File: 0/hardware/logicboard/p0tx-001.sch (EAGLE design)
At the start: 33 parts, among them IC1 LTC485N, IC2 LTC485N, IC3 LTC485N, J0 DC5V, J7 DIN5, J8 DIN5, J9 DIN5, X9 NELTRON-7810-XPXC

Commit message: Redesign.
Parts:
- removed LED2: YELLOW, led:LED3MM
- added C7: 10n, rcl:C-EU025-024X044
- added IC4: LTC485N, linear-technology:LTC485N
- added J10: DIN5, SparkFun-Connectors:DIN5
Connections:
- removed net MNTRRTN: D4.A, OK2B.C2, X9.8
- removed net MNTRSND: R4.1, X9.7
- removed net N$11: LED2.C, OK2B.VO2
- removed net N$12: LED2.A, R6L2.1
- new net MI4RTN: D4.A, J10.5, OK2B.C2
- new net MI4SND: J10.4, R4.1
- new net N$6: IC4.DI, OK2B.VO2, RN2.5
- new net TX4+: IC4.A, X9.7
- new net TX4-: IC4.B, X9.8
- net GND: now also C7.2, IC4.GND
- net VCC: now also C7.1, IC4.!RE, IC4.DE, IC4.VCC; no longer R6L2.2
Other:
- moved on the sheet: C1, C2, C3, C4, C5, C6, D4, LED1, OK2B, R4, R5L1, R6L2

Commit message: Layout.
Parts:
- removed R2, R3, R4: 220, rcl:R-EU_0204/5
- removed R5L1, R6L2, R7X, R8X: 1k, rcl:R-EU_0204/5
- added RN1: 221, resistor-dil:8R-N
- R1: value 220 -> 1k
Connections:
- net MI1SND: now also RN1A.1; no longer R1.1
- net MI2SND: now also RN1B.1; no longer R2.1
- net MI3SND: now also RN1C.1; no longer R3.1
- net MI4SND: now also RN1D.1; no longer R4.1
- net MIDIIN: now also RN1A.2; no longer R1.2
- net N$1: now also RN1D.2; no longer R4.2
- net N$4: now also R1.1; no longer R5L1.1
- net N$7: now also RN1B.2; no longer R2.2
- net N$8: now also RN1C.2; no longer R3.2
- net VCC: now also R1.2; no longer R5L1.2
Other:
- moved on the sheet: R1
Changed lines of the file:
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@@
 <part name="SUPPLY29" library="supply2" library_urn="urn:adsk.eagle:library:372" deviceset="GND" device=""/>
 <part name="X9" library="con-rj45" deviceset="NELTRON-7810-XPXC" device=""/>
-<part name="R6L2" library="rcl" library_urn="urn:adsk.eagle:library:334" deviceset="R-EU_" device="0204/5" package3d_urn="urn:adsk.eagle:package:23488/1" value="1k"/>
-<part name="R1" library="rcl" library_urn="urn:adsk.eagle:library:334" deviceset="R-EU_" device="0204/5" package3d_urn="urn:adsk.eagle:package:23488/1" value="220"/>
-<part name="R4" library="rcl" library_urn="urn:adsk.eagle:library:334" deviceset="R-EU_" device="0204/5" package3d_urn="urn:adsk.eagle:package:23488/1" value="220"/>
-<part name="R5L1" library="rcl" library_urn="urn:adsk.eagle:library:334" deviceset="R-EU_" device="0204/5" package3d_urn="urn:adsk.eagle:package:23488/1" value="1k"/>
-<part name="R2" library="rcl" library_urn="urn:adsk.eagle:library:334" deviceset="R-EU_" device="0204/5" package3d_urn="urn:adsk.eagle:package:23488/1" value="220"/>
-<part name="R3" library="rcl" library_urn="urn:adsk.eagle:library:334" deviceset="R-EU_" device="0204/5" package3d_urn="urn:adsk.eagle:package:23488/1" value="220"/>
-<part name="R7X" library="rcl" library_urn="urn:adsk.eagle:library:334" deviceset="R-EU_" device="0204/5" package3d_urn="urn:adsk.eagle:package:23488/1" value="1k"/>
-<part name="R8X" library="rcl" library_urn="urn:adsk.eagle:library:334" deviceset="R-EU_" device="0204/5" package3d_urn="urn:adsk.eagle:package:23488/1" value="1k"/>
+<part name="R1" library="rcl" library_urn="urn:adsk.eagle:library:334" deviceset="R-EU_" device="0204/5" package3d_urn="urn:adsk.eagle:package:23488/1" value="1k"/>
 <part name="OK2" library="optocoupler" library_urn="urn:adsk.eagle:library:320" deviceset="HCPL2630" device="" package3d_urn="urn:adsk.eagle:package:21941/1"/>
 <part name="D2" library="SparkFun-DiscreteSemi" library_urn="urn:adsk.eagle:library:514" deviceset="DIODE" device="-1N4148" package3d_urn="urn:adsk.eagle:package:38452/1" value=""/>
@@
 <part name="SUPPLY30" library="supply2" library_urn="urn:adsk.eagle:library:372" deviceset="VCC" device=""/>
 <part name="SUPPLY31" library="supply2" library_urn="urn:adsk.eagle:library:372" deviceset="GND" device=""/>
+<part name="RN1" library="resistor-dil" library_urn="urn:adsk.eagle:library:342" deviceset="8R-N" device="" package3d_urn="urn:adsk.eagle:package:922/2" value="221"/>
 </parts>
 <sheets>
@@
 <attribute name="VALUE" x="201.93" y="108.458" size="1.778" layer="96"/>
 </instance>
-<instance part="R6L2" gate="G$1" x="134.62" y="20.32" smashed="yes">
-<attribute name="NAME" x="130.81" y="21.8186" size="1.778" layer="95"/>
-<attribute name="VALUE" x="130.81" y="17.018" size="1.778" layer="96"/>
-</instance>
-<instance part="R1" gate="G$1" x="76.2" y="127" smashed="yes">
-<attribute name="NAME" x="72.39" y="128.4986" size="1.778" layer="95"/>
-<attribute name="VALUE" x="72.39" y="123.698" size="1.778" layer="96"/>
-</instance>
-<instance part="R4" gate="G$1" x="76.2" y="38.1" smashed="yes">
-<attribute name="NAME" x="72.39" y="39.5986" size="1.778" layer="95"/>
-<attribute name="VALUE" x="72.39" y="34.798" size="1.778" layer="96"/>
-</instance>
-<instance part="R5L1" gate="G$1" x="60.96" y="157.48" smashed="yes" rot="R90">
+<instance part="R1" gate="G$1" x="60.96" y="157.48" smashed="yes" rot="R90">
 <attribute name="NAME" x="59.4614" y="153.67" size="1.778" layer="95" rot="R90"/>
 <attribute name="VALUE" x="64.262" y="153.67" size="1.778" layer="96" rot="R90"/>
-</instance>
-<instance part="R2" gate="G$1" x="76.2" y="99.06" smashed="yes">
-<attribute name="NAME" x="72.39" y="100.5586" size="1.778" layer="95"/>
-<attribute name="VALUE" x="72.39" y="95.758" size="1.778" layer="96"/>
-</instance>
-<instance part="R3" gate="G$1" x="76.2" y="68.58" smashed="yes">
-<attribute name="NAME" x="72.39" y="70.0786" size="1.778" layer="95"/>
-<attribute name="VALUE" x="72.39" y="65.278" size="1.778" layer="96"/>
-</instance>
-<instance part="R7X" gate="G$1" x="114.3" y="22.86" smashed="yes">
-<attribute name="NAME" x="110.49" y="24.3586" size="1.778" layer="95"/>
-<attribute name="VALUE" x="110.49" y="19.558" size="1.778" layer="96"/>
-</instance>
-<instance part="R8X" gate="G$1" x="114.3" y="12.7" smashed="yes">
-<attribute name="NAME" x="110.49" y="14.1986" size="1.778" layer="95"/>
-<attribute name="VALUE" x="110.49" y="9.398" size="1.778" layer="96"/>
 </instance>
 <instance part="OK2" gate="A" x="114.3" y="66.04" smashed="yes">
@@
 <instance part="SUPPLY31" gate="GND" x="243.84" y="63.5" smashed="yes">
 <attribute name="VALUE" x="241.935" y="60.325" size="1.778" layer="96"/>
+</instance>
+<instance part="RN1" gate="A" x="76.2" y="127" smashed="yes">
+<attribute name="VALUE" x="78.74" y="123.952" size="1.778" layer="96"/>
+<attribute name="NAME" x="71.12" y="123.952" size="1.778" layer="95"/>
+</instance>
+<instance part="RN1" gate="B" x="76.2" y="99.06" smashed="yes">
+<attribute name="VALUE" x="78.74" y="96.012" size="1.778" layer="96"/>
+<attribute name="NAME" x="71.12" y="96.012" size="1.778" layer="95"/>
+</instance>
+<instance part="RN1" gate="C" x="76.2" y="68.58" smashed="yes">
+<attribute name="VALUE" x="78.74" y="65.532" size="1.778" layer="96"/>
+<attribute name="NAME" x="71.12" y="65.532" size="1.778" layer="95"/>
+</instance>
+<instance part="RN1" gate="D" x="76.2" y="38.1" smashed="yes">
+<attribute name="VALUE" x="78.74" y="35.052" size="1.778" layer="96"/>
+<attribute name="NAME" x="71.12" y="35.052" size="1.778" layer="95"/>
+</instance>
+<instance part="RN1" gate="E" x="231.14" y="124.46" smashed="yes">
+<attribute name="VALUE" x="233.68" y="121.412" size="1.778" layer="96"/>
+<attribute name="NAME" x="226.06" y="121.412" size="1.778" layer="95"/>
+</instance>
+<instance part="RN1" gate="F" x="231.14" y="119.38" smashed="yes">
+<attribute name="VALUE" x="233.68" y="116.332" size="1.778" layer="96"/>
+<attribute name="NAME" x="226.06" y="116.332" size="1.778" layer="95"/>
+</instance>
+<instance part="RN1" gate="G" x="231.14" y="114.3" smashed="yes">
+<attribute name="VALUE" x="233.68" y="111.252" size="1.778" layer="96"/>
+<attribute name="NAME" x="226.06" y="111.252" size="1.778" layer="95"/>
+</instance>
+<instance part="RN1" gate="H" x="231.14" y="109.22" smashed="yes">
+<attribute name="VALUE" x="233.68" y="106.172" size="1.778" layer="96"/>
+<attribute name="NAME" x="226.06" y="106.172" size="1.778" layer="95"/>
 </instance>
 </instances>
@@
 <segment>
 <pinref part="SUPPLY28" gate="G$1" pin="VCC"/>
-<pinref part="R5L1" gate="G$1" pin="2"/>
+<pinref part="R1" gate="G$1" pin="2"/>
 <wire x1="60.96" y1="162.56" x2="60.96" y2="165.1" width="0.1524" layer="91"/>
 </segment>
@@
 <wire x1="81.28" y1="127" x2="96.52" y2="127" width="0.1524" layer="91"/>
 <junction x="96.52" y="127"/>
-<pinref part="R1" gate="G$1" pin="2"/>
+<pinref part="RN1" gate="A" pin="2"/>
 </segment>
 </net>
@@
 <segment>
 <pinref part="J7" gate="G$1" pin="4"/>
-<pinref part="R1" gate="G$1" pin="1"/>
 <wire x1="71.12" y1="127" x2="33.02" y2="127" width="0.1524" layer="91"/>
 <label x="50.8" y="127" size="1.778" layer="95"/>
+<pinref part="RN1" gate="A" pin="1"/>
 </segment>
 </net>
@@
 <segment>
 <pinref part="J8" gate="G$1" pin="4"/>
-<pinref part="R2" gate="G$1" pin="1"/>
 <wire x1="33.02" y1="99.06" x2="71.12" y2="99.06" width="0.1524" layer="91"/>
 <label x="50.8" y="99.06" size="1.778" layer="95"/>
+<pinref part="RN1" gate="B" pin="1"/>
 </segment>
 </net>
 <net name="N$7" class="0">
 <segment>
-<pinref part="R2" gate="G$1" pin="2"/>
 <pinref part="OK1" gate="B" pin="A2"/>
 <wire x1="81.28" y1="99.06" x2="96.52" y2="99.06" width="0.1524" layer="91"/>
@@
 <wire x1="96.52" y1="96.52" x2="96.52" y2="99.06" width="0.1524" layer="91"/>
 <junction x="96.52" y="99.06"/>
+<pinref part="RN1" gate="B" pin="2"/>
 </segment>
 </net>
@@
 <segment>
 <pinref part="OK2" gate="A" pin="A1"/>
-<pinref part="R3" gate="G$1" pin="2"/>
 <wire x1="101.6" y1="68.58" x2="96.52" y2="68.58" width="0.1524" layer="91"/>
 <pinref part="D3" gate="G$1" pin="C"/>
@@
 <wire x1="96.52" y1="66.04" x2="96.52" y2="68.58" width="0.1524" layer="91"/>
 <junction x="96.52" y="68.58"/>
+<pinref part="RN1" gate="C" pin="2"/>
 </segment>
 </net>
 <net name="MI3SND" class="0">
 <segment>
-<pinref part="R3" gate="G$1" pin="1"/>
 <pinref part="J9" gate="G$1" pin="4"/>
 <wire x1="71.12" y1="68.58" x2="33.02" y2="68.58" width="0.1524" layer="91"/>
 <label x="50.8" y="68.58" size="1.778" layer="95"/>
+<pinref part="RN1" gate="C" pin="1"/>
 </segment>
 </net>
 <net name="N$1" class="0">
 <segment>
-<pinref part="R4" gate="G$1" pin="2"/>
 <pinref part="OK2" gate="B" pin="A2"/>
 <wire x1="81.28" y1="38.1" x2="96.52" y2="38.1" width="0.1524" layer="91"/>
@@
 <pinref part="D4" gate="G$1" pin="C"/>
 <wire x1="96.52" y1="35.56" x2="93.98" y2="35.56" width="0.1524" layer="91"/>
+<pinref part="RN1" gate="D" pin="2"/>
 </segment>
 </net>
@@
 <net name="N$4" class="0">
 <segment>
-<pinref part="R5L1" gate="G$1" pin="1"/>
+<pinref part="R1" gate="G$1" pin="1"/>
 <pinref part="LED1" gate="G$1" pin="A"/>
 <wire x1="60.96" y1="152.4" x2="60.96" y2="149.86" width="0.1524" layer="91"/>
@@
 <net name="MI4SND" class="0">
 <segment>
-<pinref part="R4" gate="G$1" pin="1"/>
 <pinref part="J10" gate="G$1" pin="4"/>
 <wire x1="71.12" y1="38.1" x2="33.02" y2="38.1" width="0.1524" layer="91"/>
 <label x="50.8" y="38.1" size="1.778" layer="95"/>
-</segment>
-</net>
+<pinref part="RN1" gate="D" pin="1"/>
+</segment>
+</net>

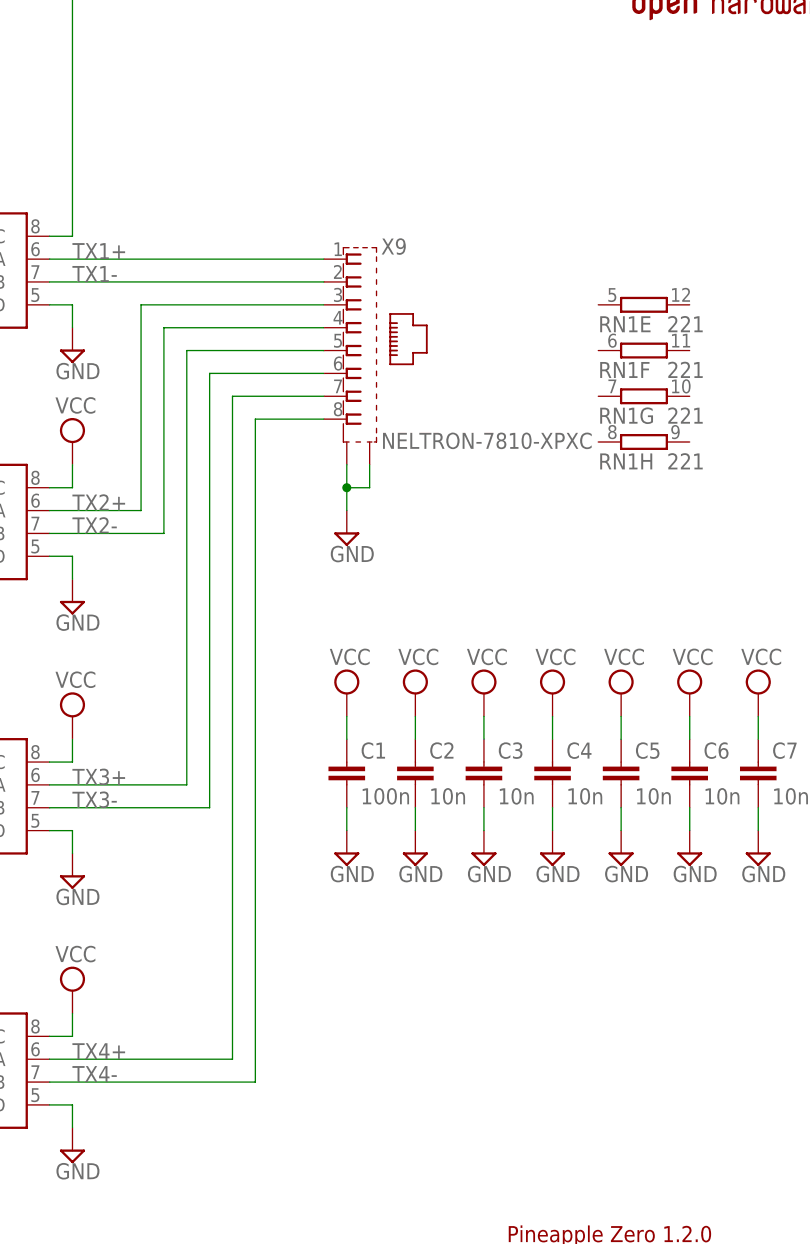
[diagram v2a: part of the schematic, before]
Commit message: Fixed wiring of 0.
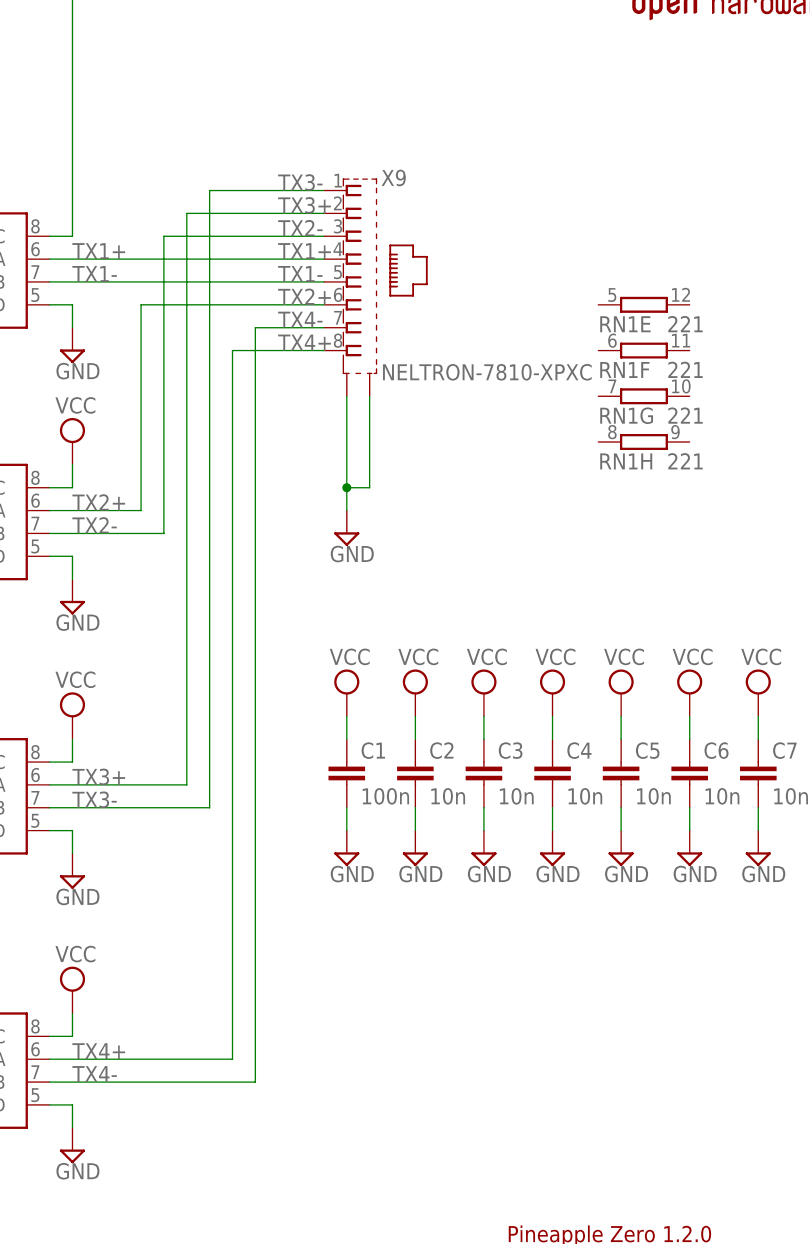
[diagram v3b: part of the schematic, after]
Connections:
- net TX1+: now also X9.4; no longer X9.1
- net TX1-: now also X9.5; no longer X9.2
- net TX2+: now also X9.6; no longer X9.3
- net TX2-: now also X9.3; no longer X9.4
- net TX3+: now also X9.2; no longer X9.5
- net TX3-: now also X9.1; no longer X9.6
- net TX4+: now also X9.8; no longer X9.7
- net TX4-: now also X9.7; no longer X9.8
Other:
- moved on the sheet: X9
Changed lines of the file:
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@@
 <attribute name="VALUE" x="59.055" y="133.985" size="1.778" layer="96"/>
 </instance>
-<instance part="X9" gate="G$1" x="198.12" y="119.38" smashed="yes">
-<attribute name="NAME" x="201.93" y="130.048" size="1.778" layer="95"/>
-<attribute name="VALUE" x="201.93" y="108.458" size="1.778" layer="96"/>
+<instance part="X9" gate="G$1" x="198.12" y="127" smashed="yes">
+<attribute name="NAME" x="201.93" y="137.668" size="1.778" layer="95"/>
+<attribute name="VALUE" x="201.93" y="116.078" size="1.778" layer="96"/>
 </instance>
 <instance part="R1" gate="G$1" x="60.96" y="157.48" smashed="yes" rot="R90">
@@
 </segment>
 <segment>
-<wire x1="198.12" y1="106.68" x2="198.12" y2="104.14" width="0.1524" layer="91"/>
+<wire x1="198.12" y1="114.3" x2="198.12" y2="104.14" width="0.1524" layer="91"/>
 <wire x1="198.12" y1="104.14" x2="200.66" y2="104.14" width="0.1524" layer="91"/>
-<wire x1="200.66" y1="104.14" x2="200.66" y2="106.68" width="0.1524" layer="91"/>
+<wire x1="200.66" y1="104.14" x2="200.66" y2="114.3" width="0.1524" layer="91"/>
 <pinref part="SUPPLY25" gate="GND" pin="GND"/>
 <wire x1="198.12" y1="104.14" x2="198.12" y2="101.6" width="0.1524" layer="91"/>
@@
 </segment>
 </net>
-<net name="TX1+" class="0">
-<segment>
-<pinref part="IC1" gate="G$1" pin="A"/>
-<wire x1="165.1" y1="129.54" x2="195.58" y2="129.54" width="0.1524" layer="91"/>
-<label x="167.64" y="129.54" size="1.778" layer="95"/>
-<pinref part="X9" gate="G$1" pin="1"/>
-</segment>
-</net>
 <net name="MIDIIN" class="0">
 <segment>
@@
 </segment>
 </net>
-<net name="TX1-" class="0">
-<segment>
-<pinref part="IC1" gate="G$1" pin="B"/>
-<wire x1="165.1" y1="127" x2="195.58" y2="127" width="0.1524" layer="91"/>
-<label x="167.64" y="127" size="1.778" layer="95"/>
-<pinref part="X9" gate="G$1" pin="2"/>
-</segment>
-</net>
 <net name="TX" class="0">
 <segment>
@@
 <net name="TX4-" class="0">
 <segment>
-<pinref part="X9" gate="G$1" pin="8"/>
-<wire x1="195.58" y1="111.76" x2="187.96" y2="111.76" width="0.1524" layer="91"/>
-<wire x1="187.96" y1="111.76" x2="187.96" y2="38.1" width="0.1524" layer="91"/>
+<wire x1="187.96" y1="121.92" x2="187.96" y2="38.1" width="0.1524" layer="91"/>
 <pinref part="IC4" gate="G$1" pin="B"/>
 <wire x1="187.96" y1="38.1" x2="165.1" y2="38.1" width="0.1524" layer="91"/>
 <label x="167.64" y="38.1" size="1.778" layer="95"/>
+<pinref part="X9" gate="G$1" pin="7"/>
+<wire x1="195.58" y1="121.92" x2="187.96" y2="121.92" width="0.1524" layer="91"/>
+<label x="190.5" y="121.92" size="1.778" layer="95"/>
 </segment>
 </net>
 <net name="TX4+" class="0">
 <segment>
-<pinref part="X9" gate="G$1" pin="7"/>
-<wire x1="195.58" y1="114.3" x2="185.42" y2="114.3" width="0.1524" layer="91"/>
-<wire x1="185.42" y1="114.3" x2="185.42" y2="40.64" width="0.1524" layer="91"/>
+<wire x1="185.42" y1="119.38" x2="185.42" y2="40.64" width="0.1524" layer="91"/>
 <pinref part="IC4" gate="G$1" pin="A"/>
 <wire x1="165.1" y1="40.64" x2="185.42" y2="40.64" width="0.1524" layer="91"/>
 <label x="167.64" y="40.64" size="1.778" layer="95"/>
+<pinref part="X9" gate="G$1" pin="8"/>
+<wire x1="195.58" y1="119.38" x2="185.42" y2="119.38" width="0.1524" layer="91"/>
+<label x="190.5" y="119.38" size="1.778" layer="95"/>
 </segment>
 </net>
@@
 <wire x1="165.1" y1="101.6" x2="175.26" y2="101.6" width="0.1524" layer="91"/>
 <wire x1="175.26" y1="101.6" x2="175.26" y2="124.46" width="0.1524" layer="91"/>
-<pinref part="X9" gate="G$1" pin="3"/>
+<label x="167.64" y="101.6" size="1.778" layer="95"/>
+<pinref part="X9" gate="G$1" pin="6"/>
 <wire x1="175.26" y1="124.46" x2="195.58" y2="124.46" width="0.1524" layer="91"/>
-<label x="167.64" y="101.6" size="1.778" layer="95"/>
+<label x="190.5" y="124.46" size="1.778" layer="95"/>
 </segment>
 </net>
@@
 <pinref part="IC2" gate="G$1" pin="B"/>
 <wire x1="165.1" y1="99.06" x2="177.8" y2="99.06" width="0.1524" layer="91"/>
-<wire x1="177.8" y1="99.06" x2="177.8" y2="121.92" width="0.1524" layer="91"/>
-<pinref part="X9" gate="G$1" pin="4"/>
-<wire x1="177.8" y1="121.92" x2="195.58" y2="121.92" width="0.1524" layer="91"/>
+<wire x1="177.8" y1="99.06" x2="177.8" y2="132.08" width="0.1524" layer="91"/>
 <label x="167.64" y="99.06" size="1.778" layer="95"/>
+<pinref part="X9" gate="G$1" pin="3"/>
+<wire x1="195.58" y1="132.08" x2="177.8" y2="132.08" width="0.1524" layer="91"/>
+<label x="190.5" y="132.08" size="1.778" layer="95"/>
 </segment>
 </net>
@@
 <pinref part="IC3" gate="G$1" pin="A"/>
 <wire x1="165.1" y1="71.12" x2="180.34" y2="71.12" width="0.1524" layer="91"/>
-<pinref part="X9" gate="G$1" pin="5"/>
-<wire x1="180.34" y1="71.12" x2="180.34" y2="119.38" width="0.1524" layer="91"/>
-<wire x1="180.34" y1="119.38" x2="195.58" y2="119.38" width="0.1524" layer="91"/>
+<wire x1="180.34" y1="71.12" x2="180.34" y2="134.62" width="0.1524" layer="91"/>
 <label x="167.64" y="71.12" size="1.778" layer="95"/>
+<pinref part="X9" gate="G$1" pin="2"/>
+<wire x1="195.58" y1="134.62" x2="180.34" y2="134.62" width="0.1524" layer="91"/>
+<label x="190.5" y="134.62" size="1.778" layer="95"/>
 </segment>
 </net>
@@
 <pinref part="IC3" gate="G$1" pin="B"/>
 <wire x1="165.1" y1="68.58" x2="182.88" y2="68.58" width="0.1524" layer="91"/>
-<pinref part="X9" gate="G$1" pin="6"/>
-<wire x1="182.88" y1="68.58" x2="182.88" y2="116.84" width="0.1524" layer="91"/>
-<wire x1="182.88" y1="116.84" x2="195.58" y2="116.84" width="0.1524" layer="91"/>
+<wire x1="182.88" y1="68.58" x2="182.88" y2="137.16" width="0.1524" layer="91"/>
 <label x="167.64" y="68.58" size="1.778" layer="95"/>
+<pinref part="X9" gate="G$1" pin="1"/>
+<wire x1="195.58" y1="137.16" x2="182.88" y2="137.16" width="0.1524" layer="91"/>
+<label x="190.5" y="137.16" size="1.778" layer="95"/>
 </segment>
 </net>
@@
 </segment>
 </net>
+<net name="TX1+" class="0">
+<segment>
+<pinref part="IC1" gate="G$1" pin="A"/>
+<pinref part="X9" gate="G$1" pin="4"/>
+<wire x1="165.1" y1="129.54" x2="195.58" y2="129.54" width="0.1524" layer="91"/>
+<label x="190.5" y="129.54" size="1.778" layer="95"/>
+<label x="167.64" y="129.54" size="1.778" layer="95"/>
+</segment>
+</net>
+<net name="TX1-" class="0">
+<segment>
+<pinref part="IC1" gate="G$1" pin="B"/>
+<pinref part="X9" gate="G$1" pin="5"/>
+<wire x1="165.1" y1="127" x2="195.58" y2="127" width="0.1524" layer="91"/>
+<label x="190.5" y="127" size="1.778" layer="95"/>
+<label x="167.64" y="127" size="1.778" layer="95"/>
+</segment>
+</net>
